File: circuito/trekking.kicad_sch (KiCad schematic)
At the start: 46 parts, among them J1 Raspberry Pi, J10 P2, J11 P3, J12 I2C0, J13 I2C0, J14 I2C0, J15 I2C0, J16 I2C0, J17 I2C0, J18 Module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

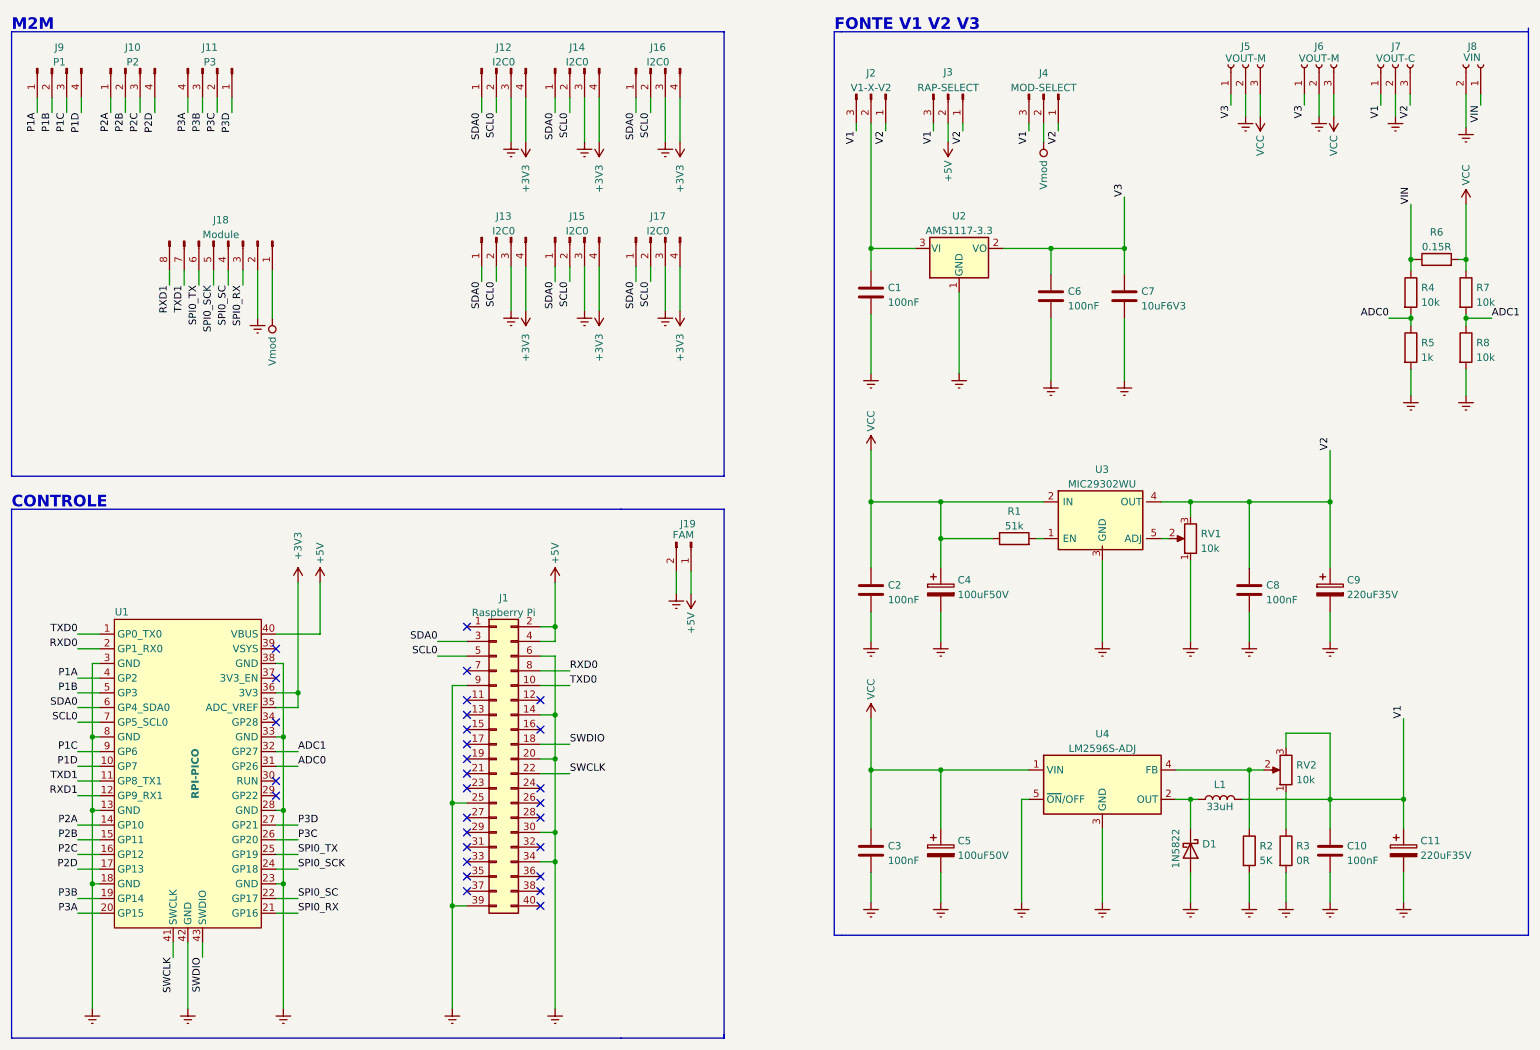
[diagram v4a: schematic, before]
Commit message: ATT placa fontes e pinos de contole
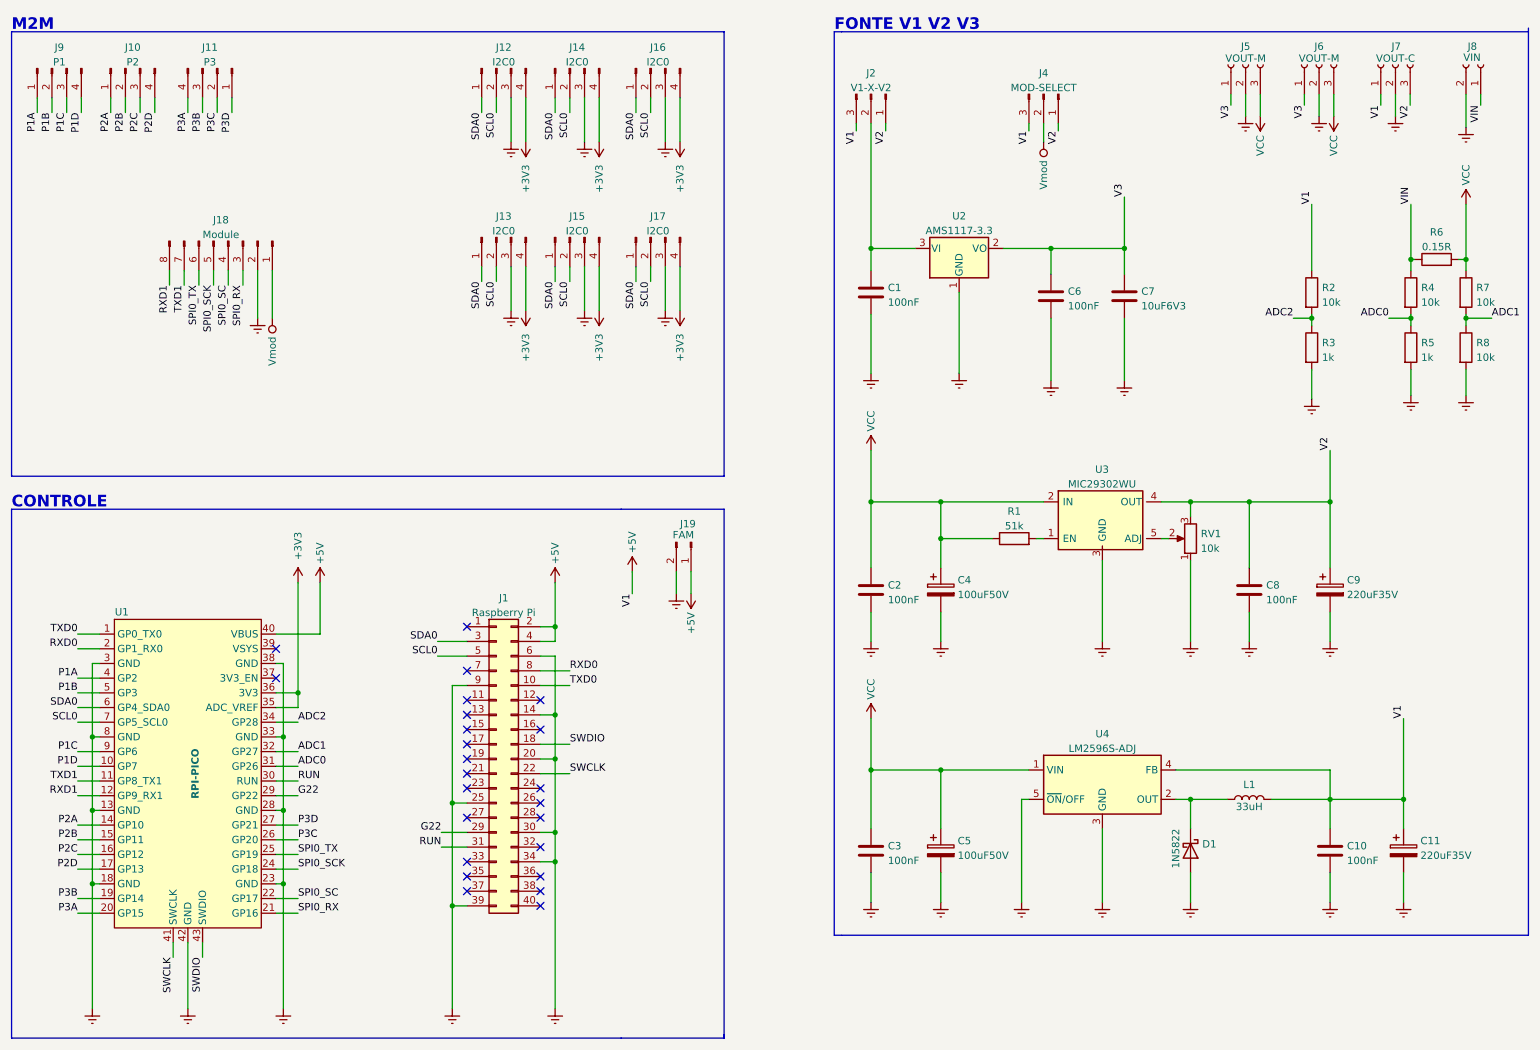
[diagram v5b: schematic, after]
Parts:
- removed J3: RAP-SELECT, Connector_PinHeader_2.54mm:PinHeader_1x03_P2.54mm_Vertical, symbol Connector:Conn_01x03_Male
- removed RV2: 10k, Potentiometer_THT:Potentiometer_Bourns_3266Y_Vertical, symbol Device:R_Potentiometer
- R2: value 5K -> 10k
- R3: value 0R -> 1k
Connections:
- net V1 is gone; now on net +5V: C10.1, C11.1, J2.3 (Pin_3), J4.3 (Pin_3), J7.1 (Pin_1), L1.2
- net +5V: now also R2.1, U4.4 (FB)
- net Earth: no longer R2.2
- net G22: now reaches J1.29 (Pin_29)
- net G22: now also U1.29 (GP22)
- net RUN: now reaches J1.31 (Pin_31)
- net RUN: now also U1.30 (RUN)
- net ADC2: now reaches R3.1
- net ADC2: now also R2.2, U1.34 (GP28)
- no-connect marks 29 -> 24
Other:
- moved on the sheet: L1

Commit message: update
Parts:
- U4: value LM2596S-ADJ -> LM2596S-5.0
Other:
- moved on the sheet: R2, R3
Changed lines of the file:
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@@
   (junction (at 64.135 153.035) (diameter 0) (color 0 0 0 0)
   )
-  (junction (at 241.935 67.945) (diameter 0) (color 0 0 0 0)
+  (junction (at 240.665 67.945) (diameter 0) (color 0 0 0 0)
   )
   (junction (at 245.11 151.13) (diameter 0) (color 0 0 0 0)
@@
     (stroke (width 0) (type default) (color 0 0 0 0))
   )
-  (wire (pts (xy 241.935 76.835) (xy 241.935 81.915))
+  (wire (pts (xy 240.665 76.835) (xy 240.665 81.915))
     (stroke (width 0) (type default) (color 0 0 0 0))
   )
@@
     (stroke (width 0) (type default) (color 0 0 0 0))
   )
-  (wire (pts (xy 241.935 67.31) (xy 241.935 67.945))
+  (wire (pts (xy 240.665 67.31) (xy 240.665 67.945))
     (stroke (width 0) (type default) (color 0 0 0 0))
   )
@@
     (stroke (width 0) (type default) (color 0 0 0 0))
   )
-  (wire (pts (xy 241.935 67.945) (xy 241.935 69.215))
+  (wire (pts (xy 240.665 67.945) (xy 240.665 69.215))
     (stroke (width 0) (type default) (color 0 0 0 0))
   )
@@
     (stroke (width 0) (type default) (color 0 0 0 0))
   )
-  (wire (pts (xy 238.76 67.945) (xy 241.935 67.945))
+  (wire (pts (xy 237.49 67.945) (xy 240.665 67.945))
     (stroke (width 0) (type default) (color 0 0 0 0))
   )
@@
     (stroke (width 0) (type default) (color 0 0 0 0))
   )
-  (wire (pts (xy 241.935 48.26) (xy 241.935 59.69))
+  (wire (pts (xy 240.665 48.26) (xy 240.665 59.69))
     (stroke (width 0) (type default) (color 0 0 0 0))
   )
@@
     (effects (font (size 1.27 1.27)) (justify right bottom))
   )
-  (label "ADC2" (at 238.76 67.945 180)
+  (label "ADC2" (at 237.49 67.945 180)
     (effects (font (size 1.27 1.27)) (justify right bottom))
   )
@@
     (effects (font (size 1.27 1.27)) (justify right bottom))
   )
-  (label "V1" (at 241.935 48.26 90)
+  (label "V1" (at 240.665 48.26 90)
     (effects (font (size 1.27 1.27)) (justify left bottom))
   )
@@
     (in_bom yes) (on_board yes) (fields_autoplaced)
     (property "Reference" "U4" (id 0) (at 205.74 139.8102 0))
-    (property "Value" "LM2596S-ADJ" (id 1) (at 205.74 142.3471 0))
+    (property "Value" "LM2596S-5.0" (id 1) (at 205.74 142.3471 0))
     (property "Footprint" "Package_TO_SOT_SMD:TO-263-5_TabPin3" (id 2) (at 207.01 154.94 0)
       (effects (font (size 1.27 1.27) italic) (justify left) hide)
@@
     (pin "1")
   )
-  (symbol (lib_id "Device:R") (at 241.935 73.025 0) (unit 1)
-    (in_bom yes) (on_board yes) (fields_autoplaced)
-    (property "Reference" "R3" (id 0) (at 243.713 72.1903 0)
-      (effects (font (size 1.27 1.27)) (justify left))
-    )
-    (property "Value" "1k" (id 1) (at 243.713 74.7272 0)
-      (effects (font (size 1.27 1.27)) (justify left))
-    )
-    (property "Footprint" "Resistor_SMD:R_0805_2012Metric_Pad1.20x1.40mm_HandSolder" (id 2) (at 240.157 73.025 90)
-      (effects (font (size 1.27 1.27)) hide)
-    )
-    (property "Datasheet" "~" (id 3) (at 241.935 73.025 0)
+  (symbol (lib_id "Device:R") (at 240.665 73.025 0) (unit 1)
+    (in_bom yes) (on_board yes) (fields_autoplaced)
+    (property "Reference" "R3" (id 0) (at 242.443 72.1903 0)
+      (effects (font (size 1.27 1.27)) (justify left))
+    )
+    (property "Value" "1k" (id 1) (at 242.443 74.7272 0)
+      (effects (font (size 1.27 1.27)) (justify left))
+    )
+    (property "Footprint" "Resistor_SMD:R_0805_2012Metric_Pad1.20x1.40mm_HandSolder" (id 2) (at 238.887 73.025 90)
+      (effects (font (size 1.27 1.27)) hide)
+    )
+    (property "Datasheet" "~" (id 3) (at 240.665 73.025 0)
       (effects (font (size 1.27 1.27)) hide)
     )
@@
     (pin "3")
   )
-  (symbol (lib_id "Device:R") (at 241.935 63.5 0) (unit 1)
-    (in_bom yes) (on_board yes) (fields_autoplaced)
-    (property "Reference" "R2" (id 0) (at 243.713 62.6653 0)
-      (effects (font (size 1.27 1.27)) (justify left))
-    )
-    (property "Value" "10k" (id 1) (at 243.713 65.2022 0)
-      (effects (font (size 1.27 1.27)) (justify left))
-    )
-    (property "Footprint" "Resistor_SMD:R_0805_2012Metric_Pad1.20x1.40mm_HandSolder" (id 2) (at 240.157 63.5 90)
-      (effects (font (size 1.27 1.27)) hide)
-    )
-    (property "Datasheet" "~" (id 3) (at 241.935 63.5 0)
-      (effects (font (size 1.27 1.27)) hide)
-    )
-    (pin "1")
-    (pin "2")
-  )
-  (symbol (lib_id "power:Earth") (at 241.935 81.915 0) (unit 1)
-    (in_bom yes) (on_board yes) (fields_autoplaced)
-    (property "Reference" "#PWR01" (id 0) (at 241.935 88.265 0)
-      (effects (font (size 1.27 1.27)) hide)
-    )
-    (property "Value" "Earth" (id 1) (at 241.935 85.725 0)
-      (effects (font (size 1.27 1.27)) hide)
-    )
-    (property "Footprint" "" (id 2) (at 241.935 81.915 0)
-      (effects (font (size 1.27 1.27)) hide)
-    )
-    (property "Datasheet" "~" (id 3) (at 241.935 81.915 0)
+  (symbol (lib_id "Device:R") (at 240.665 63.5 0) (unit 1)
+    (in_bom yes) (on_board yes) (fields_autoplaced)
+    (property "Reference" "R2" (id 0) (at 242.443 62.6653 0)
+      (effects (font (size 1.27 1.27)) (justify left))
+    )
+    (property "Value" "10k" (id 1) (at 242.443 65.2022 0)
+      (effects (font (size 1.27 1.27)) (justify left))
+    )
+    (property "Footprint" "Resistor_SMD:R_0805_2012Metric_Pad1.20x1.40mm_HandSolder" (id 2) (at 238.887 63.5 90)
+      (effects (font (size 1.27 1.27)) hide)
+    )
+    (property "Datasheet" "~" (id 3) (at 240.665 63.5 0)
+      (effects (font (size 1.27 1.27)) hide)
+    )
+    (pin "1")
+    (pin "2")
+  )
+  (symbol (lib_id "power:Earth") (at 240.665 81.915 0) (unit 1)
+    (in_bom yes) (on_board yes) (fields_autoplaced)
+    (property "Reference" "#PWR01" (id 0) (at 240.665 88.265 0)
+      (effects (font (size 1.27 1.27)) hide)
+    )
+    (property "Value" "Earth" (id 1) (at 240.665 85.725 0)
+      (effects (font (size 1.27 1.27)) hide)
+    )
+    (property "Footprint" "" (id 2) (at 240.665 81.915 0)
+      (effects (font (size 1.27 1.27)) hide)
+    )
+    (property "Datasheet" "~" (id 3) (at 240.665 81.915 0)
       (effects (font (size 1.27 1.27)) hide)
     )
@@
     )
     (path "/4138cb08-195d-46f7-bdb8-11ae75932dca"
-      (reference "U4") (unit 1) (value "LM2596S-ADJ") (footprint "Package_TO_SOT_SMD:TO-263-5_TabPin3")
-    )
-  )
+      (reference "U4") (unit 1) (value "LM2596S-5.0") (footprint "Package_TO_SOT_SMD:TO-263-5_TabPin3")
+    )
+  )

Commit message: fwe d_motor_SDK tst pwm
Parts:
- R8: value 10k -> 1k
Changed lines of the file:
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@@
   (symbol (lib_id "Device:R") (at 268.605 73.025 0) (unit 1)
     (in_bom yes) (on_board yes) (fields_autoplaced)
-    (property "Reference" "R8" (id 0) (at 270.383 72.1903 0)
-      (effects (font (size 1.27 1.27)) (justify left))
-    )
-    (property "Value" "10k" (id 1) (at 270.383 74.7272 0)
+    (property "Reference" "R8" (id 0) (at 270.51 71.7549 0)
+      (effects (font (size 1.27 1.27)) (justify left))
+    )
+    (property "Value" "1k" (id 1) (at 270.51 74.2949 0)
       (effects (font (size 1.27 1.27)) (justify left))
     )
@@
     )
     (path "/bcde46da-460b-4d5c-b420-c61b19384d5c"
-      (reference "R8") (unit 1) (value "10k") (footprint "Resistor_SMD:R_0805_2012Metric_Pad1.20x1.40mm_HandSolder")
+      (reference "R8") (unit 1) (value "1k") (footprint "Resistor_SMD:R_0805_2012Metric_Pad1.20x1.40mm_HandSolder")
     )
     (path "/e53c495b-ccc4-4ea3-acf4-dbbcfa72990d"
